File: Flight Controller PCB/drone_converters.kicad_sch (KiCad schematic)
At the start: 10 parts, among them U5 LDL212DR, U6 LDL212DR

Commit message: Selected motor controller, fixed MCU schematic and added I2C pullups
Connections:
- net +3V3: no longer C24.1, R12.2, U6.1 (VOUT)
- new net +1V8: C24.1, R12.2, U6.1 (VOUT)

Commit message: Some changes. TODO: Add power and control for RunCam2. Add battery voltage monitoring
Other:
- moved on the sheet: C21, C22, C23, C24, R10, R11, R12, R13, U5, U6

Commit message: Updated gitignore
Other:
- moved on the sheet: C21, C22, C23, C24, R10, R11, R12, R13, U5, U6

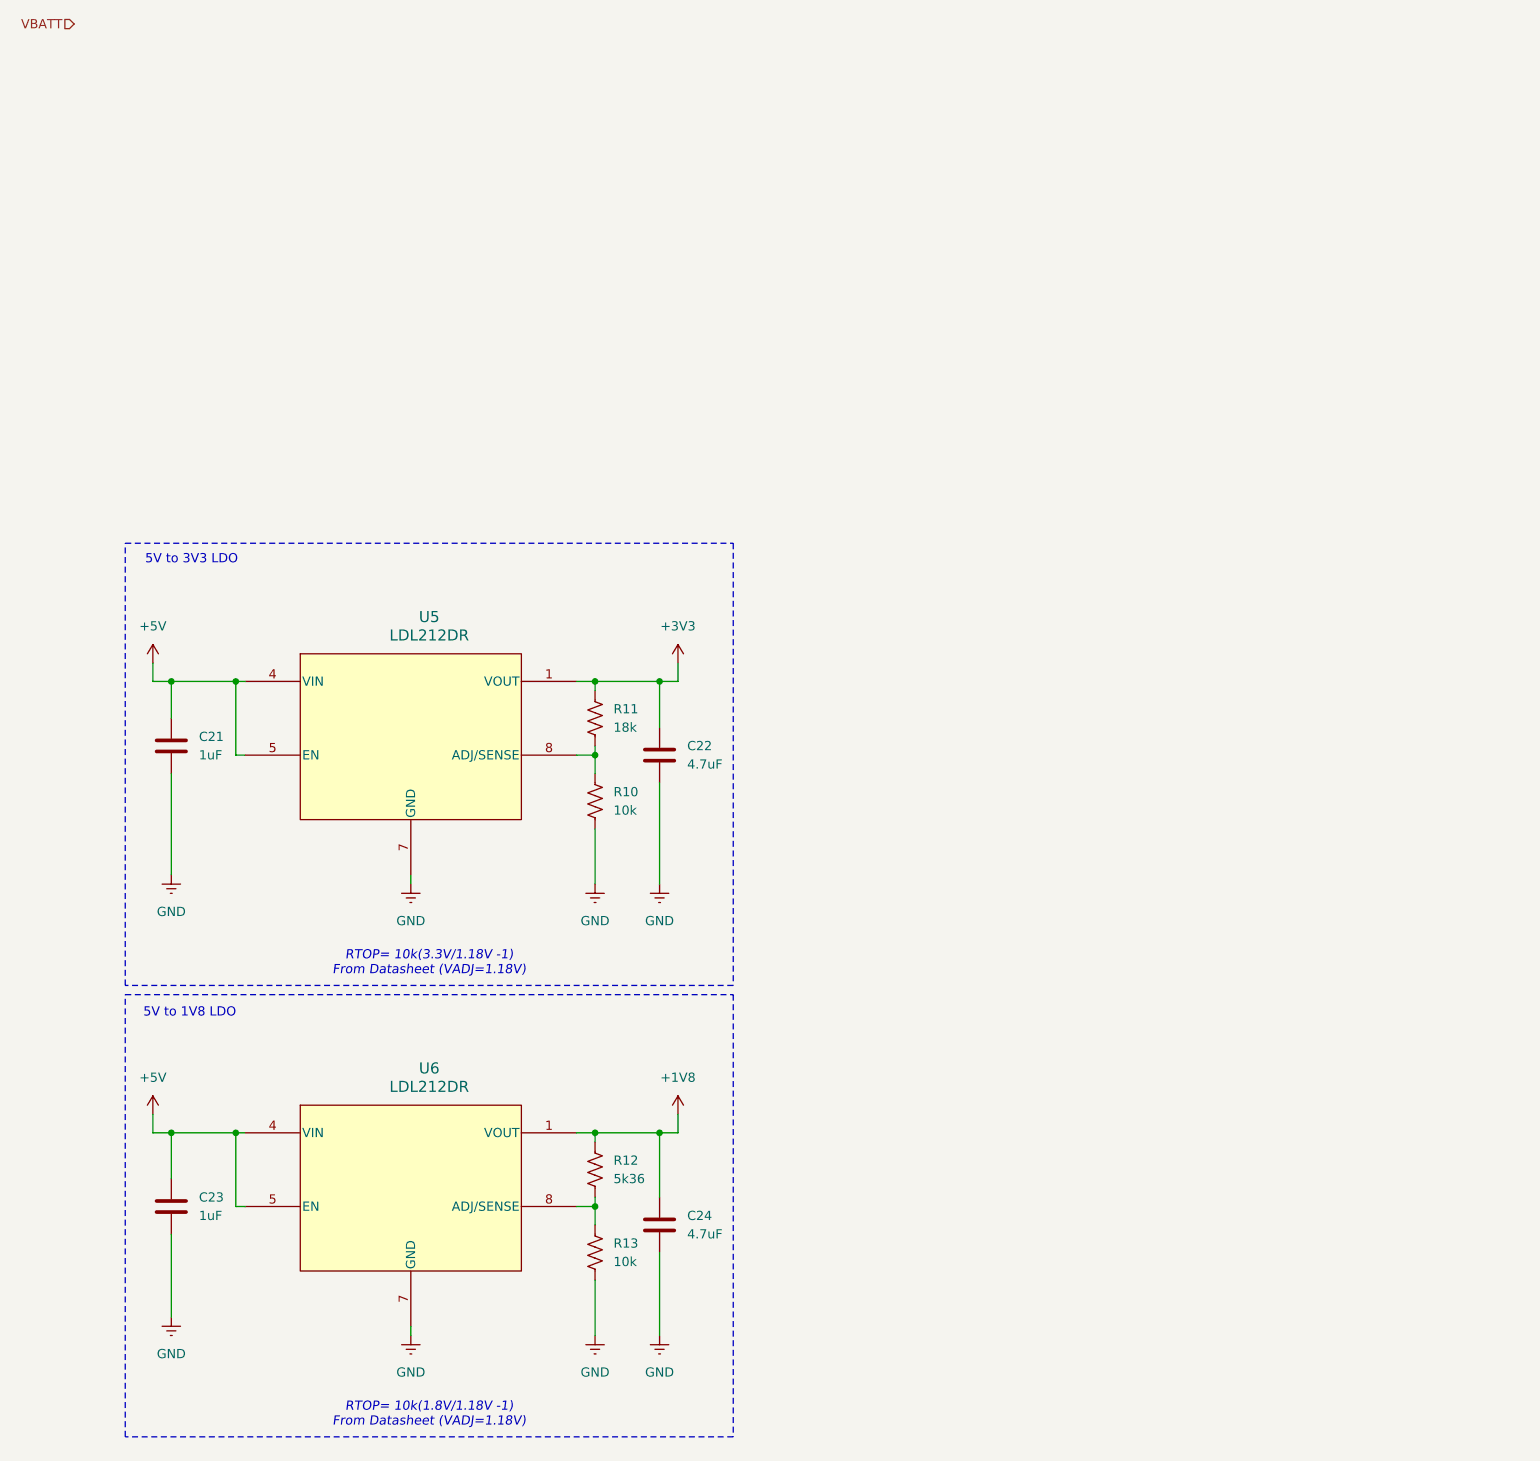
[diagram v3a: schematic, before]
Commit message: Finished converters, combined converter & sensor sheets. Updated I2C & CS pullups. TODO: Add motor control pins to MCU & control pins for camera
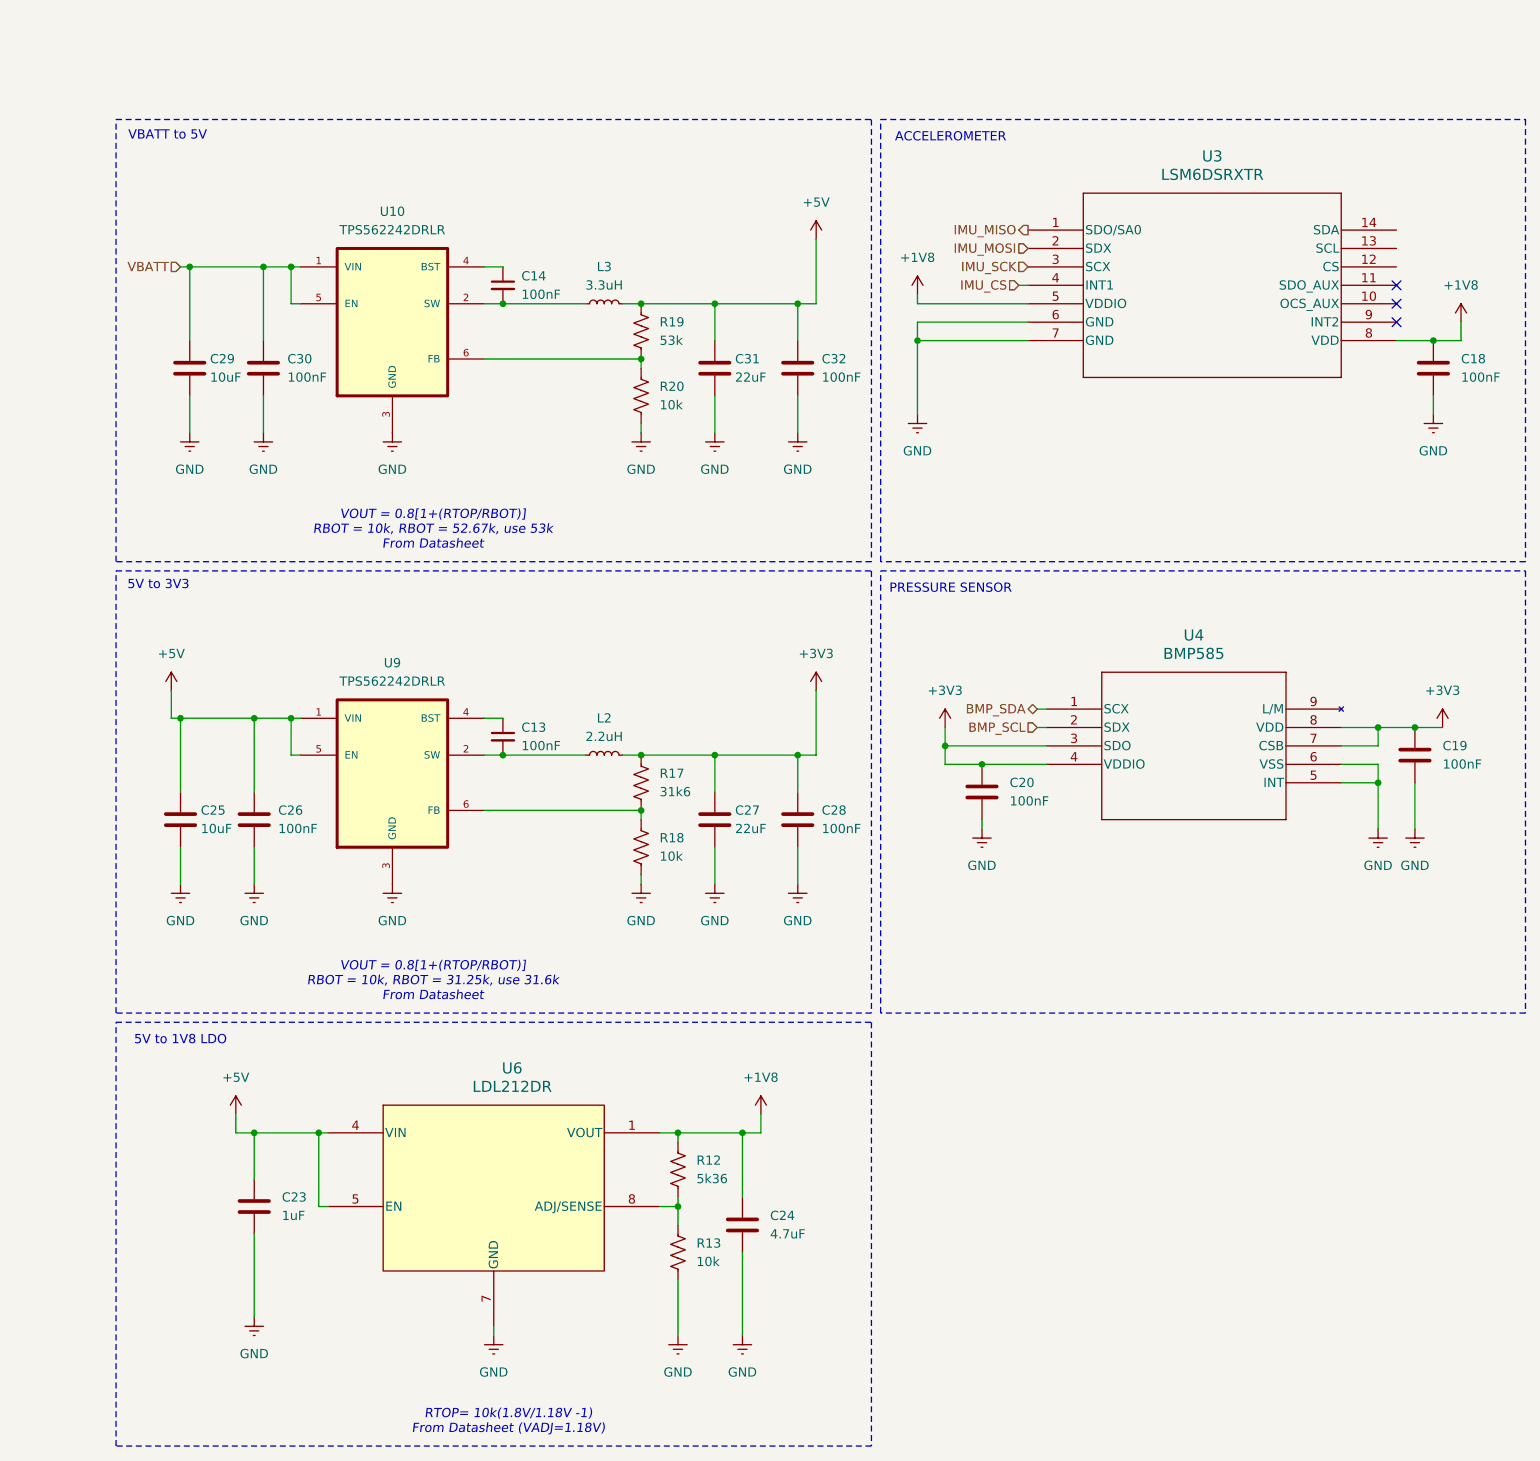
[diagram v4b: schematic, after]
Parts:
- removed C21: 1uF, Capacitor_SMD:C_0603_1608Metric, symbol Device:C
- removed C22: 4.7uF, Capacitor_SMD:C_0603_1608Metric, symbol Device:C
- removed R10: 10k, Resistor_SMD:R_0603_1608Metric, symbol Device:R_US
- removed R11: 18k, Resistor_SMD:R_0603_1608Metric, symbol Device:R_US
- removed U5: LDL212DR, Drone_Fp:SO8B_4X5X1P27_STM, symbol Drone_sym:LDL212DR
- added C13, C14: 100nF, symbol Device:C_Small
- added C18, C19, C20, C26, C28, C30, C32: 100nF, Capacitor_SMD:C_0603_1608Metric, symbol Device:C
- added C25, C29: 10uF, Capacitor_SMD:C_0603_1608Metric, symbol Device:C
- added C27, C31: 22uF, Capacitor_SMD:C_0603_1608Metric, symbol Device:C
- added L2: 2.2uH, symbol Device:L_Small
- added L3: 3.3uH, symbol Device:L_Small
- added R17: 31k6, Resistor_SMD:R_0603_1608Metric, symbol Device:R_US
- added R18, R20: 10k, Resistor_SMD:R_0603_1608Metric, symbol Device:R_US
- added R19: 53k, Resistor_SMD:R_0603_1608Metric, symbol Device:R_US
- added U10, U9: TPS562242DRLR, Drone_Fp:SOT50P160X60-6N, symbol Drone_sym:TPS562242DRLR
- added U3: LSM6DSRXTR, Drone_Fp:LGA-14L_STM, symbol Drone_sym:LSM6DSRXTR
- added U4: BMP585, Drone_Fp:LGA9_BMP585_BOS, symbol Drone_sym:BMP585
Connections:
- net +1V8: now also C18.1, U3.5 (VDDIO), U3.8 (VDD)
- net +3V3: now also C19.1, C20.1, C27.1, C28.1, L2.2, R17.2, U4.3 (SDO), U4.4 (VDDIO), U4.7 (CSB), U4.8 (VDD)
- net +5V: now also C25.1, C26.1, C31.1, C32.1, L3.2, R19.2, U9.1 (VIN), U9.5 (EN)
- net GND: now also C18.2, C19.2, C20.2, C25.2, C26.2, C27.2, C28.2, C29.2, C30.2, C31.2, C32.2, R18.1, R20.1, U10.3 (GND), U3.6 (GND), U3.7 (GND), U4.5 (INT), U4.6 (VSS), U9.3 (GND)
- net VBATT: now also C29.1, C30.1, U10.1 (VIN), U10.5 (EN)
- new net: C13.2, L2.1, U9.2 (SW)
- new net: C14.2, L3.1, U10.2 (SW)
- new net: C14.1, U10.4 (BST)
- new net: R19.1, R20.2, U10.6 (FB)
- new net: R17.1, R18.2, U9.6 (FB)
- new net: C13.1, U9.4 (BST)
- new net BMP_SCL: U4.2 (SDX)
- new net BMP_SDA: U4.1 (SCX)
- new net IMU_CS: U3.4 (INT1)
- new net IMU_MISO: U3.1 (SDO/SA0)
- new net IMU_MOSI: U3.2 (SDX)
- new net IMU_SCK: U3.3 (SCX)
- no-connect marks 0 -> 3
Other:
- note added: "5V to 3V3"
- note added: "ACCELEROMETER"
- note added: "PRESSURE SENSOR"
- note added: "VBATT to 5V"
- note added: "VOUT = 0.8[1+(RTOP/RBOT)] RBOT = 10k, RBOT = 31.25k, use 31.6k From Datasheet"
- note added: "VOUT = 0.8[1+(RTOP/RBOT)] RBOT = 10k, RBOT = 52.67k, use 53k From Datasheet"
- note removed: "5V to 3V3 LDO"
- note removed: "RTOP= 10k(3.3V/1.18V -1) From Datasheet (VADJ=1.18V)"
- moved on the sheet: C23, C24, R12, R13, U6

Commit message: Init
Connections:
- net IMU_CS: now also U3.12 (CS); no longer U3.4 (INT1)
- net 1V8_ADJ: now reaches R12.1, R13.2, U6.8 (ADJ/SENSE)
- net 5V_FB: now reaches R19.1, R20.2, U10.6 (FB)
- net 3V3_FB: now reaches R17.1, R18.2, U9.6 (FB)
- no-connect marks 3 -> 6
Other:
- moved on the sheet: C23, C24, R12, R13, U6
